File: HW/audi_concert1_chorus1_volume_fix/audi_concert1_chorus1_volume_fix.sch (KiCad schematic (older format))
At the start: 44 parts, among them CON1 I2C_to_TDA, CON2 USB, CON3 SPI_TO_PANEL, CON4 JLINK, SW1 SWITCH_DPST, U1 68HC05_PLCC, U2 AP1117-33, U3 STM32F103C8Tx, Y1 Crystal_GND24, Y2 Crystal_GND24

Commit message: move hw files
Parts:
- removed C1: 1uF, Capacitors_SMD.pretty:C_1206_HandSoldering, symbol c:C
- removed R1: 100k, Resistors_SMD.pretty:R_0805_HandSoldering, symbol Device:R
- removed R21: 2k2, Resistors_SMD.pretty:R_0805_HandSoldering, symbol Device:R
- removed R22: 3k3, Resistors_SMD.pretty:R_0805_HandSoldering, symbol Device:R
- removed SW1: SWITCH_DPST, modules:3x6x2.5mm_tact_switch, symbol MiscellaneousDevices:SWITCH_DPST
- C2, C3, C4, C5, C6, C7: symbol c:C -> audi_concert1_chorus1_volume_fix-rescue:C-c
- CON1: symbol con:CONN_2 -> audi_concert1_chorus1_volume_fix-rescue:CONN_2-con
- CON2: symbol con:CONN_4 -> audi_concert1_chorus1_volume_fix-rescue:CONN_4-con
- CON3: symbol con:CONN_3 -> audi_concert1_chorus1_volume_fix-rescue:CONN_3-con
- CON4: symbol Connectors:CONN_1x6 -> audi_concert1_chorus1_volume_fix-rescue:CONN_1x6-Connectors
- U1: symbol 68HC05:68HC05_PLCC -> audi_concert1_chorus1_volume_fix-rescue:68HC05_PLCC-68HC05
- U2: symbol Regulator_Linear:AP1117-33 -> audi_concert1_chorus1_volume_fix-rescue:AP1117-33-Regulator_Linear
- U3: symbol MCU_ST_STM32:STM32F103C8Tx -> audi_concert1_chorus1_volume_fix-rescue:STM32F103C8Tx-MCU_ST_STM32
- Y1: value Crystal_GND24 -> 32.768kHz
- Y2: value Crystal_GND24 -> 8MHz
- gave numbers to parts that had none: 1
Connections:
- net 3V3: now also U4.3 (VCC)
- net 5V: now also CON2.1; no longer CON2.4
- net GND: now also CON2.4; no longer CON2.1
- net RESET_MOTO: no longer U4.3 (VCC)
- net USB+: no longer R12.1, R14.2
- net USB-: no longer R13.2
- new net: R12.1, R14.2
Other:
- note removed: "3V when reset of moto goes to 5V"
- note removed: "not populated"
- moved on the sheet: R12, R13, R14, U4

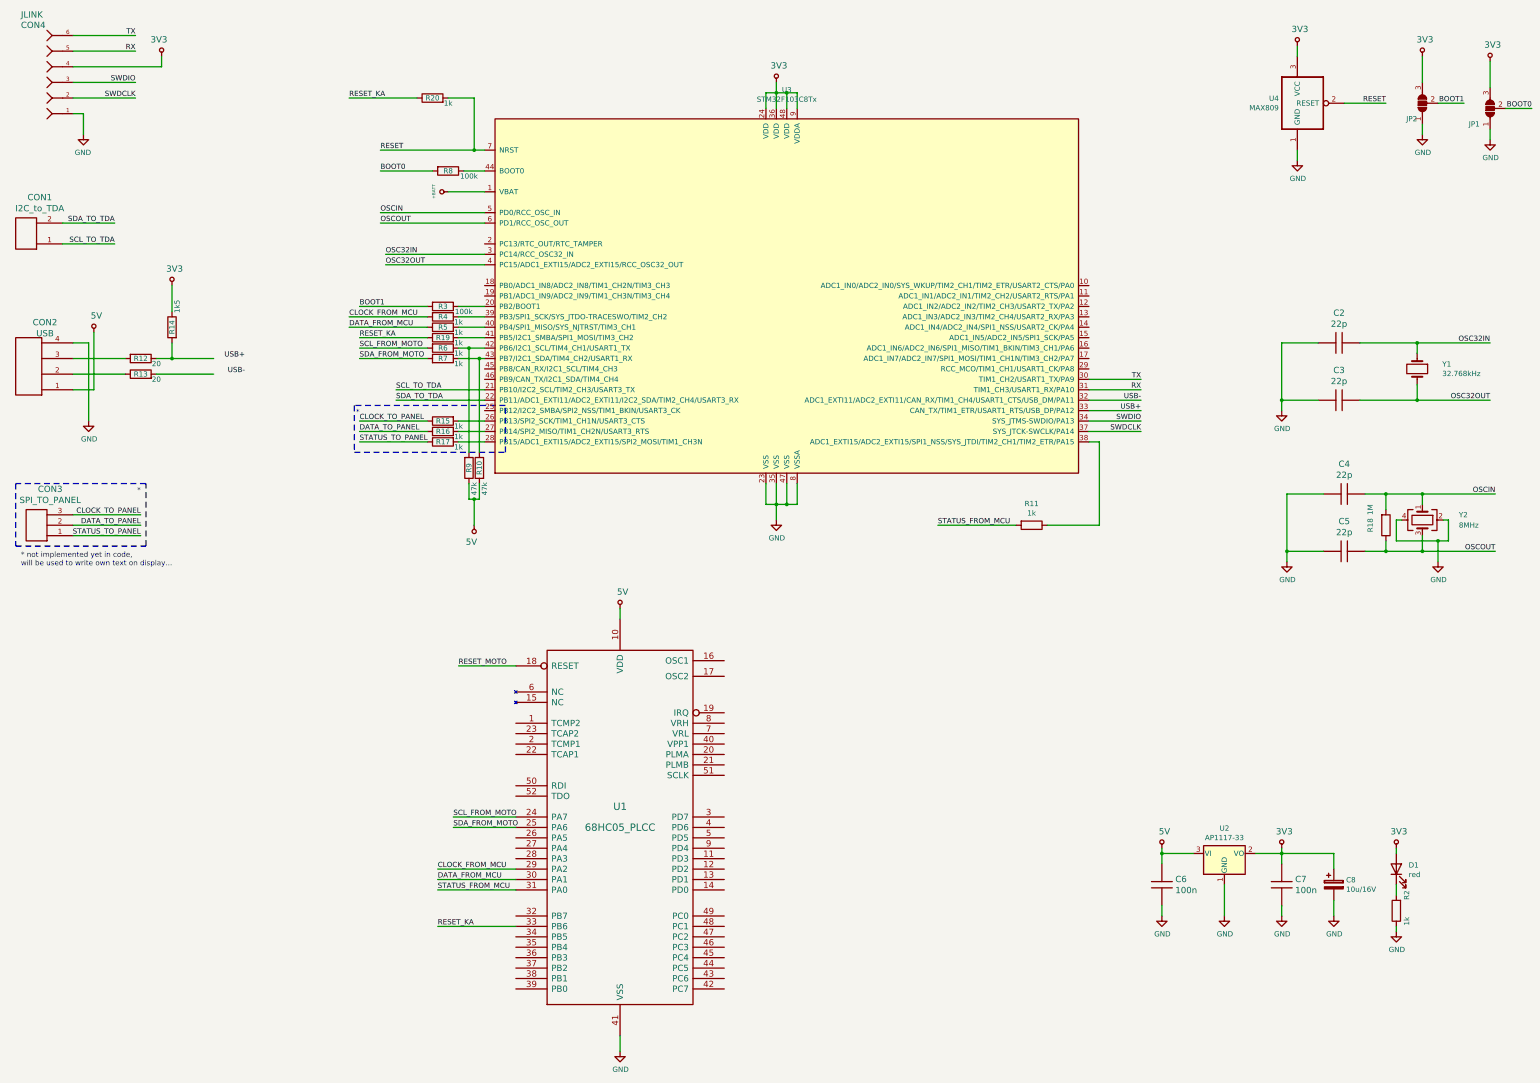
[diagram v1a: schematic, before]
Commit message: HW part for GALA support
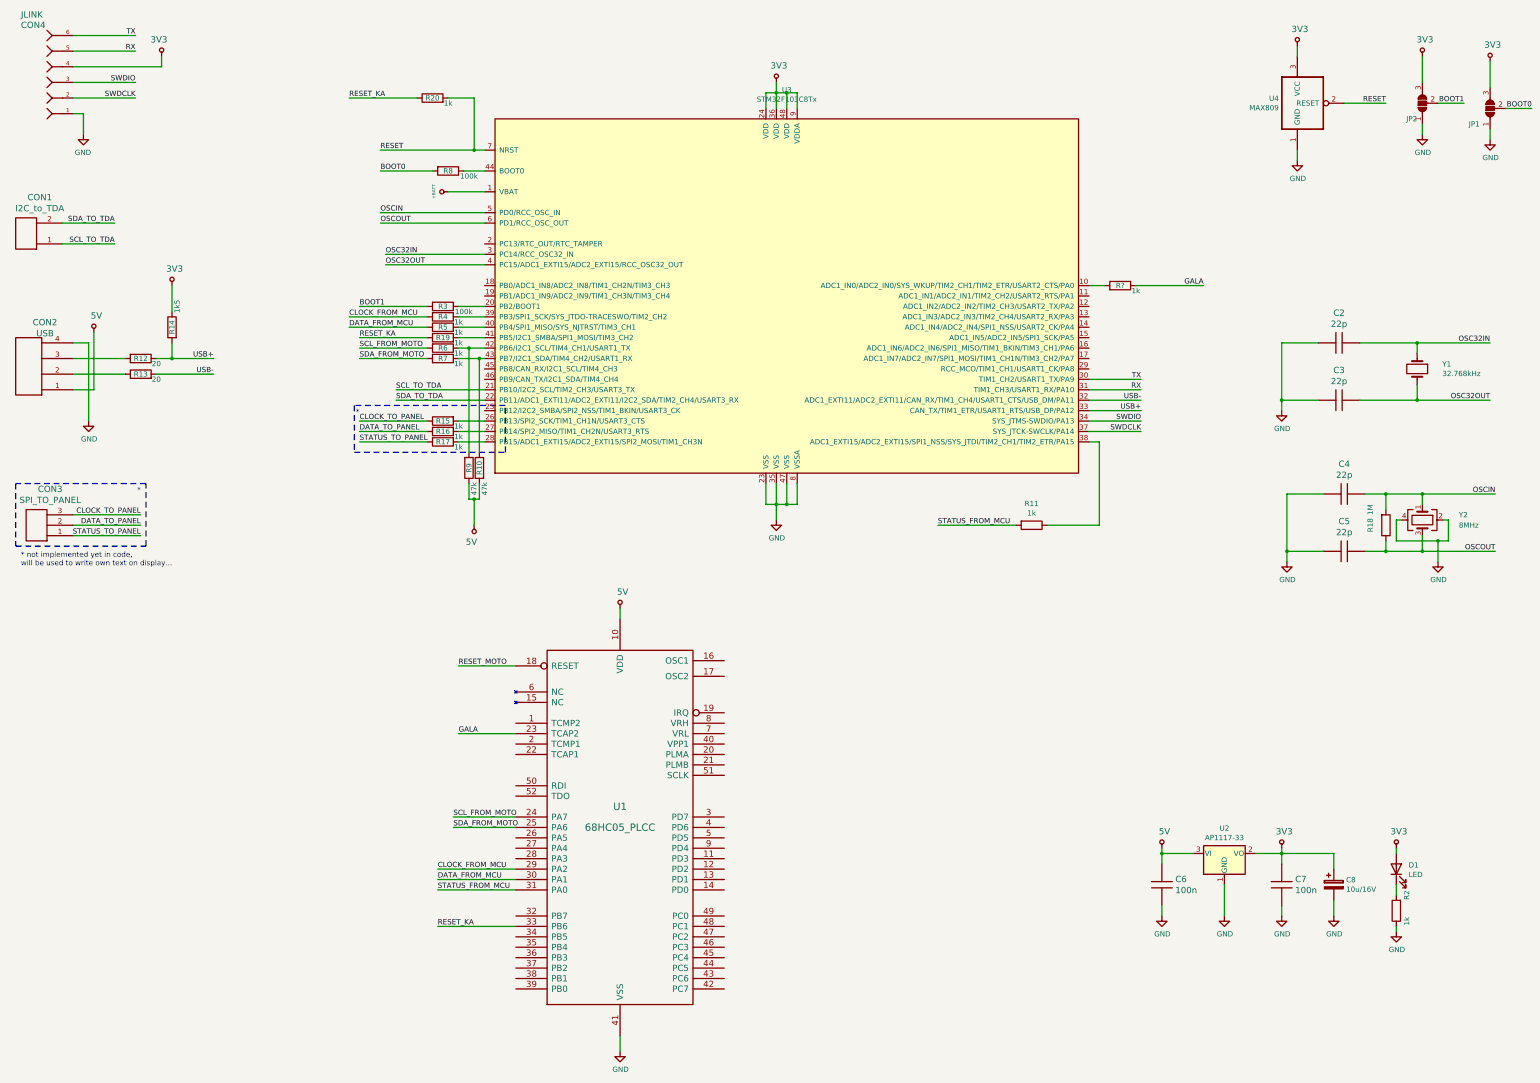
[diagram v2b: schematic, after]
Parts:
- added R?: 1k, Resistors_SMD.pretty:R_0805_HandSoldering, symbol Device:R
- D1: value red -> LED
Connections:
- net USB+: now also R12.1, R14.2
- net USB-: now also R13.2
- net GALA: now reaches U1.23 (TCAP2)
- net GALA: now also R?.1
- net at U3.10 (ADC1_IN0/ADC2_IN0/SYS_WKUP/TIM2_CH1/TIM2_ETR/USART2_CTS/PA0): now also R?.2
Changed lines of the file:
@@
 $EndComp
-Wire Wire Line
-	14450 1800 14450 1700
 Wire Wire Line
 	8150 5150 8150 5350
@@
 	1    0    0    -1
 $EndComp
-Wire Wire Line
-	15100 1850 15100 1750
 $Comp
 L audi_concert1_chorus1_volume_fix-rescue:3V3-pwr #PWR0112
@@
 Text Label 15500 1550 2    50   ~ 0
 BOOT0
-Wire Wire Line
-	15500 1550 15250 1550
 Text Label 14850 1500 2    50   ~ 0
 BOOT1
-Wire Wire Line
-	14600 1500 14850 1500
 $Comp
 L Device:LED D1
@@
 P 14200 8850
 F 0 "D1" V 14238 8732 50  0000 R CNN
-F 1 "red" V 14147 8732 50  0000 R CNN
+F 1 "LED" V 14147 8732 50  0000 R CNN
 F 2 "LEDs.pretty:LED-1206" H 14200 8850 50  0001 C CNN
 F 3 "~" H 14200 8850 50  0001 C CNN
@@
 Wire Wire Line
 	2300 3950 2450 3950
-Text Label 3150 3950 2    50   ~ 0
+Text Label 2850 3950 2    50   ~ 0
 USB+
-Text Label 3150 4100 2    50   ~ 0
+Text Label 2850 4100 2    50   ~ 0
 USB-
 Wire Wire Line
@@
 	1    0    0    -1
 $EndComp
+Wire Wire Line
+	14450 1700 14450 1800
+Wire Wire Line
+	14600 1500 14850 1500
+Wire Wire Line
+	15250 1550 15500 1550
+Wire Wire Line
+	15100 1750 15100 1850
+Wire Wire Line
+	5750 7550 5200 7550
+Text Label 5200 7550 0    50   ~ 0
+GALA
+Wire Wire Line
+	11250 3250 11400 3250
+$Comp
+L Device:R R?
+U 1 1 5C9B88B9
+P 11550 3250
+F 0 "R?" V 11550 3250 50  0000 C CNN
+F 1 "1k" V 11500 3400 50  0000 C CNN
+F 2 "Resistors_SMD.pretty:R_0805_HandSoldering" V 11480 3250 50  0001 C CNN
+F 3 "~" H 11550 3250 50  0001 C CNN
+	1    11550 3250
+	0    1    -1   0
+$EndComp
+Wire Wire Line
+	11700 3250 12350 3250
+Text Label 12350 3250 2    50   ~ 0
+GALA
 $EndSCHEMATC

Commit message: gala support in HW
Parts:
- gave numbers to parts that had none: 1
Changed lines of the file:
@@
 	11250 3250 11400 3250
 $Comp
-L Device:R R?
+L Device:R R1
 U 1 1 5C9B88B9
 P 11550 3250
-F 0 "R?" V 11550 3250 50  0000 C CNN
+F 0 "R1" V 11550 3250 50  0000 C CNN
 F 1 "1k" V 11500 3400 50  0000 C CNN
 F 2 "Resistors_SMD.pretty:R_0805_HandSoldering" V 11480 3250 50  0001 C CNN
